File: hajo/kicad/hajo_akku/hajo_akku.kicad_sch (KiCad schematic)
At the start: 18 parts, among them J1 Seetalk NG, J2 Batteries, J4 Device type, U1 MCP2562, U2 LF50CV

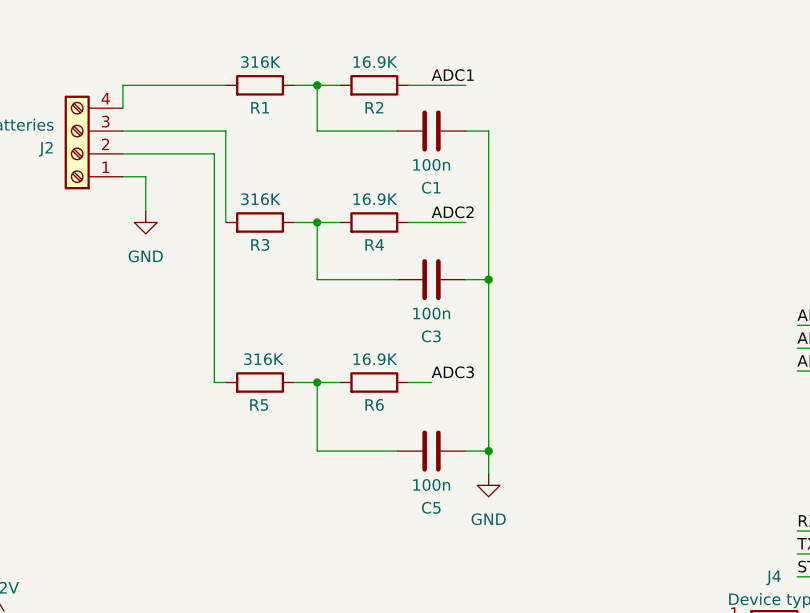
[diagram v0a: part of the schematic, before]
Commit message: kicad fix schematic
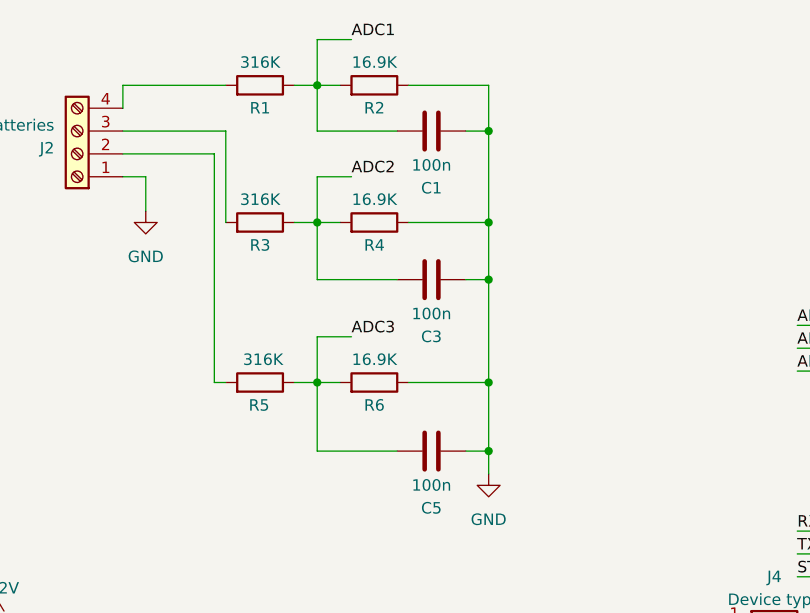
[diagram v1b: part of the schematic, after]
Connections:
- net ADC1: now also C1.2, R1.1, R2.2; no longer R2.1
- net ADC2: now also C3.2, R3.1, R4.2; no longer R4.1
- net ADC3: now also C5.2, R5.1, R6.2; no longer R6.1
- net GND: now also R2.1, R4.1, R6.1
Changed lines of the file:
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@@
   (junction (at 162.56 86.36) (diameter 0) (color 0 0 0 0)
   )
+  (junction (at 137.16 39.37) (diameter 0) (color 0 0 0 0)
+  )
   (junction (at 54.61 73.66) (diameter 0) (color 0 0 0 0)
   )
@@
   )
   (junction (at 25.4 73.66) (diameter 0) (color 0 0 0 0)
+  )
+  (junction (at 137.16 57.15) (diameter 0) (color 0 0 0 0)
+  )
+  (junction (at 137.16 29.21) (diameter 0) (color 0 0 0 0)
   )
   (junction (at 162.56 91.44) (diameter 0) (color 0 0 0 0)
@@
     (stroke (width 0) (type default))
   )
-  (wire (pts (xy 128.27 57.15) (xy 130.81 57.15))
-    (stroke (width 0) (type default))
-  )
   (wire (pts (xy 82.55 86.36) (xy 85.09 86.36))
     (stroke (width 0) (type default))
@@
     (stroke (width 0) (type default))
   )
-  (wire (pts (xy 137.16 45.72) (xy 137.16 64.77))
+  (wire (pts (xy 137.16 45.72) (xy 137.16 57.15))
     (stroke (width 0) (type default))
   )
@@
     (stroke (width 0) (type default))
   )
+  (wire (pts (xy 118.11 19.05) (xy 121.92 19.05))
+    (stroke (width 0) (type default))
+  )
   (wire (pts (xy 171.45 50.8) (xy 179.07 50.8))
     (stroke (width 0) (type default))
@@
     (stroke (width 0) (type default))
   )
+  (wire (pts (xy 118.11 24.13) (xy 118.11 19.05))
+    (stroke (width 0) (type default))
+  )
   (wire (pts (xy 107.95 39.37) (xy 107.95 29.21))
     (stroke (width 0) (type default))
@@
     (stroke (width 0) (type default))
   )
-  (wire (pts (xy 128.27 24.13) (xy 134.62 24.13))
-    (stroke (width 0) (type default))
-  )
   (wire (pts (xy 25.4 86.36) (xy 40.64 86.36))
     (stroke (width 0) (type default))
@@
     (stroke (width 0) (type default))
   )
+  (wire (pts (xy 137.16 57.15) (xy 137.16 64.77))
+    (stroke (width 0) (type default))
+  )
   (wire (pts (xy 85.09 96.52) (xy 82.55 96.52))
     (stroke (width 0) (type default))
@@
     (stroke (width 0) (type default))
   )
+  (wire (pts (xy 128.27 57.15) (xy 137.16 57.15))
+    (stroke (width 0) (type default))
+  )
+  (wire (pts (xy 128.27 24.13) (xy 137.16 24.13))
+    (stroke (width 0) (type default))
+  )
+  (wire (pts (xy 118.11 34.29) (xy 121.92 34.29))
+    (stroke (width 0) (type default))
+  )
   (wire (pts (xy 67.31 39.37) (xy 74.93 39.37))
     (stroke (width 0) (type default))
   )
+  (wire (pts (xy 118.11 39.37) (xy 118.11 34.29))
+    (stroke (width 0) (type default))
+  )
   (wire (pts (xy 120.65 24.13) (xy 118.11 24.13))
     (stroke (width 0) (type default))
   )
+  (wire (pts (xy 118.11 52.07) (xy 121.92 52.07))
+    (stroke (width 0) (type default))
+  )
   (wire (pts (xy 106.68 57.15) (xy 106.68 31.75))
     (stroke (width 0) (type default))
@@
     (stroke (width 0) (type default))
   )
-  (wire (pts (xy 137.16 29.21) (xy 137.16 45.72))
+  (wire (pts (xy 137.16 29.21) (xy 137.16 39.37))
     (stroke (width 0) (type default))
   )
@@
     (stroke (width 0) (type default))
   )
+  (wire (pts (xy 137.16 24.13) (xy 137.16 29.21))
+    (stroke (width 0) (type default))
+  )
   (wire (pts (xy 191.77 27.94) (xy 191.77 33.02))
     (stroke (width 0) (type default))
@@
     (stroke (width 0) (type default))
   )
+  (wire (pts (xy 118.11 57.15) (xy 118.11 52.07))
+    (stroke (width 0) (type default))
+  )
   (wire (pts (xy 96.52 24.13) (xy 96.52 26.67))
     (stroke (width 0) (type default))
   )
+  (wire (pts (xy 137.16 39.37) (xy 137.16 45.72))
+    (stroke (width 0) (type default))
+  )
   (wire (pts (xy 107.95 57.15) (xy 106.68 57.15))
     (stroke (width 0) (type default))
@@
     (stroke (width 0) (type default))
   )
-  (wire (pts (xy 128.27 39.37) (xy 134.62 39.37))
+  (wire (pts (xy 128.27 39.37) (xy 137.16 39.37))
     (stroke (width 0) (type default))
   )
@@
     (effects (font (size 1.27 1.27)) (justify left bottom))
   )
-  (label "ADC2" (at 130.81 39.37 0) (fields_autoplaced)
+  (label "ADC2" (at 121.92 34.29 0) (fields_autoplaced)
     (effects (font (size 1.27 1.27)) (justify left bottom))
   )
@@
     (effects (font (size 1.27 1.27)) (justify left bottom))
   )
-  (label "ADC1" (at 130.81 24.13 0) (fields_autoplaced)
-    (effects (font (size 1.27 1.27)) (justify left bottom))
-  )
-  (label "ADC3" (at 130.81 57.15 0) (fields_autoplaced)
-    (effects (font (size 1.27 1.27)) (justify left bottom))
-  )
+  (label "ADC1" (at 121.92 19.05 0) (fields_autoplaced)
+    (effects (font (size 1.27 1.27)) (justify left bottom))
+  )
+  (label "ADC3" (at 121.92 52.07 0) (fields_autoplaced)
+    (effects (font (size 1.27 1.27)) (justify left bottom))
+  )

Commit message: final pcb
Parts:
- removed J4: Device type, Connector_PinHeader_2.54mm:PinHeader_2x04_P2.54mm_Vertical, symbol Connector_Generic:Conn_02x04_Odd_Even
- added H1, H2, H3, H4: MountingHole, MountingHole:MountingHole_3.2mm_M3, symbol Mechanical:MountingHole
- added J3: Terminator, Connector_PinHeader_2.54mm:PinHeader_2x02_P2.54mm_Vertical, symbol Connector_Generic:Conn_02x02_Odd_Even
- U2: footprint Package_TO_SOT_THT:TO-220-3_Vertical -> Package_TO_SOT_THT:TO-220-3_Horizontal_TabDown
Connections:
- net CANH: now also J3.1 (Pin_1); no longer R7.1
- net CANL: now also J3.3 (Pin_3); no longer R7.2
- net GND: now also A1.16 (GPIO14/ADC2_3), J1.4 (Pin_4)
- new net: J3.2 (Pin_2), R7.1
- new net: J3.4 (Pin_4), R7.2
- no-connect marks 29 -> 31
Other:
- note added: "Shield"
- moved on the sheet: R7

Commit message: final pcb
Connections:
- net GND: now also A1.12 (GPIO10/ADC1_9); no longer A1.16 (GPIO14/ADC2_3)
- net RXD: now also A1.17 (GPIO15/ADC2_4/U0RTS); no longer A1.12 (GPIO10/ADC1_9)
- net STBY: now also A1.19 (GPIO17/ADC2_6/U1TXD); no longer A1.14 (GPIO12/ADC2_1)
- net TXD: now also A1.18 (GPIO16/ADC2_5/U0CTS); no longer A1.13 (GPIO11/ADC2_0)
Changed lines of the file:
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@@
   (junction (at 118.11 57.15) (diameter 0) (color 0 0 0 0)
   )
-  (no_connect (at 179.07 88.9))
+  (no_connect (at 179.07 78.74))
   (no_connect (at 229.87 78.74))
   (no_connect (at 229.87 66.04))
@@
   (no_connect (at 229.87 55.88))
   (no_connect (at 229.87 73.66))
-  (no_connect (at 179.07 86.36))
   (no_connect (at 229.87 93.98))
   (no_connect (at 229.87 86.36))
@@
   (no_connect (at 179.07 58.42))
   (no_connect (at 179.07 63.5))
+  (no_connect (at 179.07 83.82))
   (no_connect (at 229.87 68.58))
   (no_connect (at 229.87 58.42))
-  (no_connect (at 179.07 91.44))
+  (no_connect (at 179.07 76.2))
   (no_connect (at 179.07 71.12))
   (no_connect (at 179.07 68.58))
@@
     (stroke (width 0) (type default))
   )
-  (wire (pts (xy 171.45 76.2) (xy 179.07 76.2))
+  (wire (pts (xy 171.45 88.9) (xy 179.07 88.9))
     (stroke (width 0) (type default))
   )
@@
     (stroke (width 0) (type default))
   )
-  (wire (pts (xy 162.56 83.82) (xy 162.56 95.25))
-    (stroke (width 0) (type default))
-  )
   (wire (pts (xy 118.11 45.72) (xy 118.11 39.37))
     (stroke (width 0) (type default))
@@
     (stroke (width 0) (type default))
   )
-  (wire (pts (xy 162.56 83.82) (xy 179.07 83.82))
+  (wire (pts (xy 162.56 73.66) (xy 179.07 73.66))
     (stroke (width 0) (type default))
   )
@@
     (stroke (width 0) (type default))
   )
-  (wire (pts (xy 171.45 78.74) (xy 179.07 78.74))
+  (wire (pts (xy 171.45 91.44) (xy 179.07 91.44))
     (stroke (width 0) (type default))
   )
@@
     (stroke (width 0) (type default))
   )
-  (wire (pts (xy 171.45 73.66) (xy 179.07 73.66))
+  (wire (pts (xy 171.45 86.36) (xy 179.07 86.36))
     (stroke (width 0) (type default))
   )
@@
     (effects (font (size 1.27 1.27)) (justify left bottom))
   )
-  (label "RXD" (at 171.45 73.66 0) (fields_autoplaced)
+  (label "RXD" (at 171.45 86.36 0) (fields_autoplaced)
     (effects (font (size 1.27 1.27)) (justify left bottom))
   )
@@
     (effects (font (size 1.27 1.27)) (justify left bottom))
   )
-  (label "TXD" (at 171.45 76.2 0) (fields_autoplaced)
+  (label "TXD" (at 171.45 88.9 0) (fields_autoplaced)
     (effects (font (size 1.27 1.27)) (justify left bottom))
   )
@@
     (effects (font (size 1.27 1.27)) (justify left bottom))
   )
-  (label "STBY" (at 171.45 78.74 0) (fields_autoplaced)
+  (label "STBY" (at 171.45 91.44 0) (fields_autoplaced)
     (effects (font (size 1.27 1.27)) (justify left bottom))
   )
@@
     )
   )
-  (symbol (lib_id "power:GND") (at 162.56 95.25 0) (unit 1)
-    (in_bom yes) (on_board yes) (dnp no) (fields_autoplaced)
-    (property "Reference" "#PWR014" (at 162.56 101.6 0)
-      (effects (font (size 1.27 1.27)) hide)
-    )
-    (property "Value" "GND" (at 162.56 100.33 0)
-      (effects (font (size 1.27 1.27)))
-    )
-    (property "Footprint" "" (at 162.56 95.25 0)
-      (effects (font (size 1.27 1.27)) hide)
-    )
-    (property "Datasheet" "" (at 162.56 95.25 0)
-      (effects (font (size 1.27 1.27)) hide)
-    )
+  (symbol (lib_id "power:GND") (at 162.56 73.66 0) (unit 1)
+    (in_bom yes) (on_board yes) (dnp no) (fields_autoplaced)
+    (property "Reference" "#PWR014" (at 162.56 80.01 0)
+      (effects (font (size 1.27 1.27)) hide)
+    )
+    (property "Value" "GND" (at 162.56 78.74 0)
+      (effects (font (size 1.27 1.27)))
+    )
+    (property "Footprint" "" (at 162.56 73.66 0)
+      (effects (font (size 1.27 1.27)) hide)
+    )
+    (property "Datasheet" "" (at 162.56 73.66 0)
+      (effects (font (size 1.27 1.27)) hide)
+    )

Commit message: fix akku
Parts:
- U1: footprint Package_DIP:DIP-8_W7.62mm -> Package_DIP:DIP-8_W7.62mm_Socket
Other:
- moved on the sheet: C3, C5, R3, R4, R5, R6

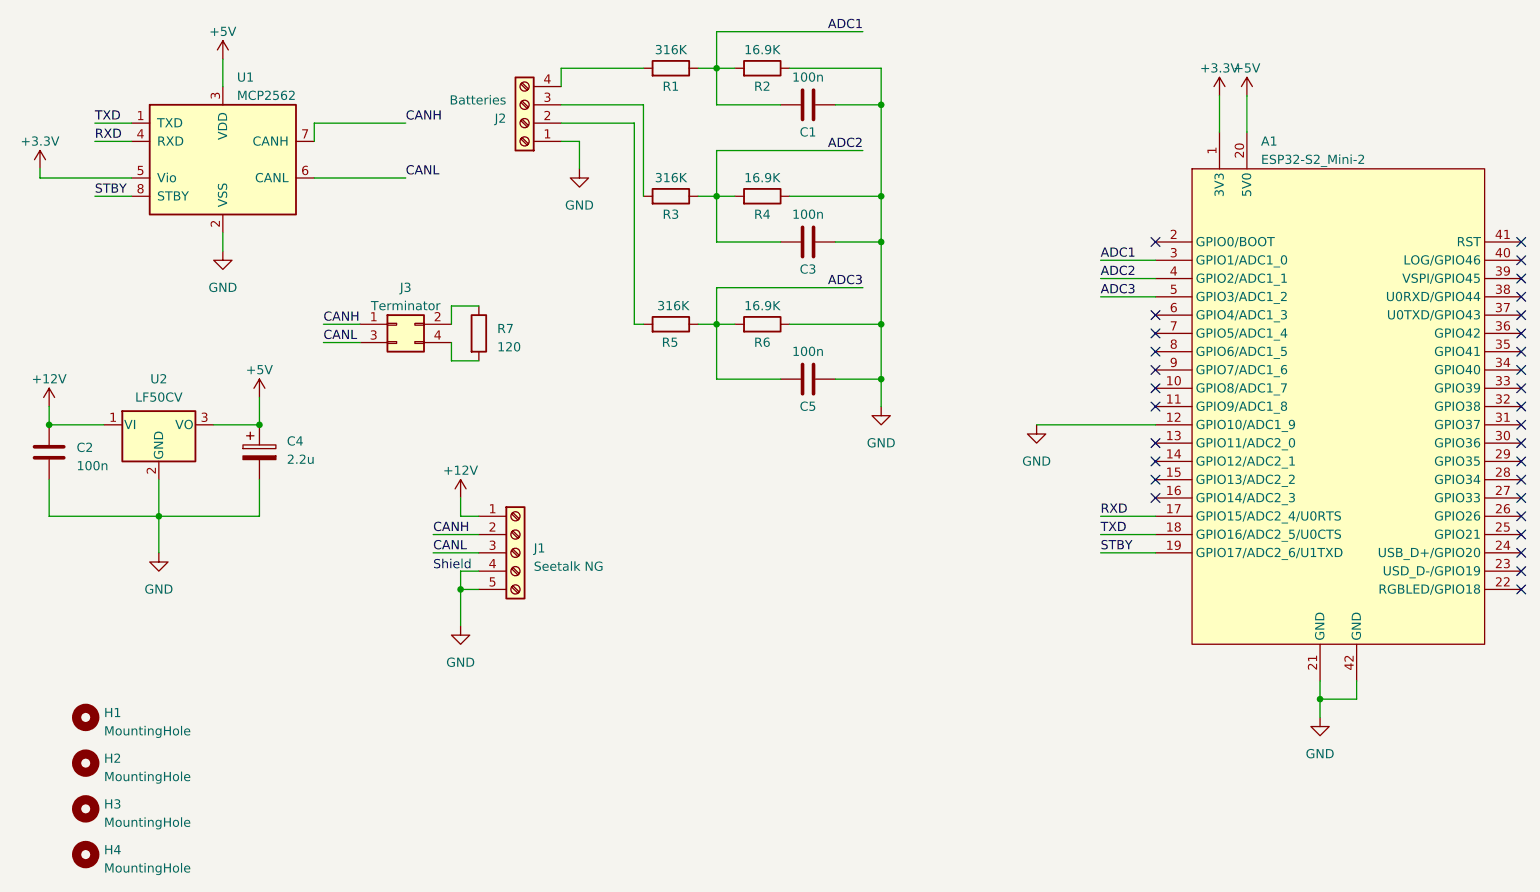
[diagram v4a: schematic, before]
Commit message: akku on new board
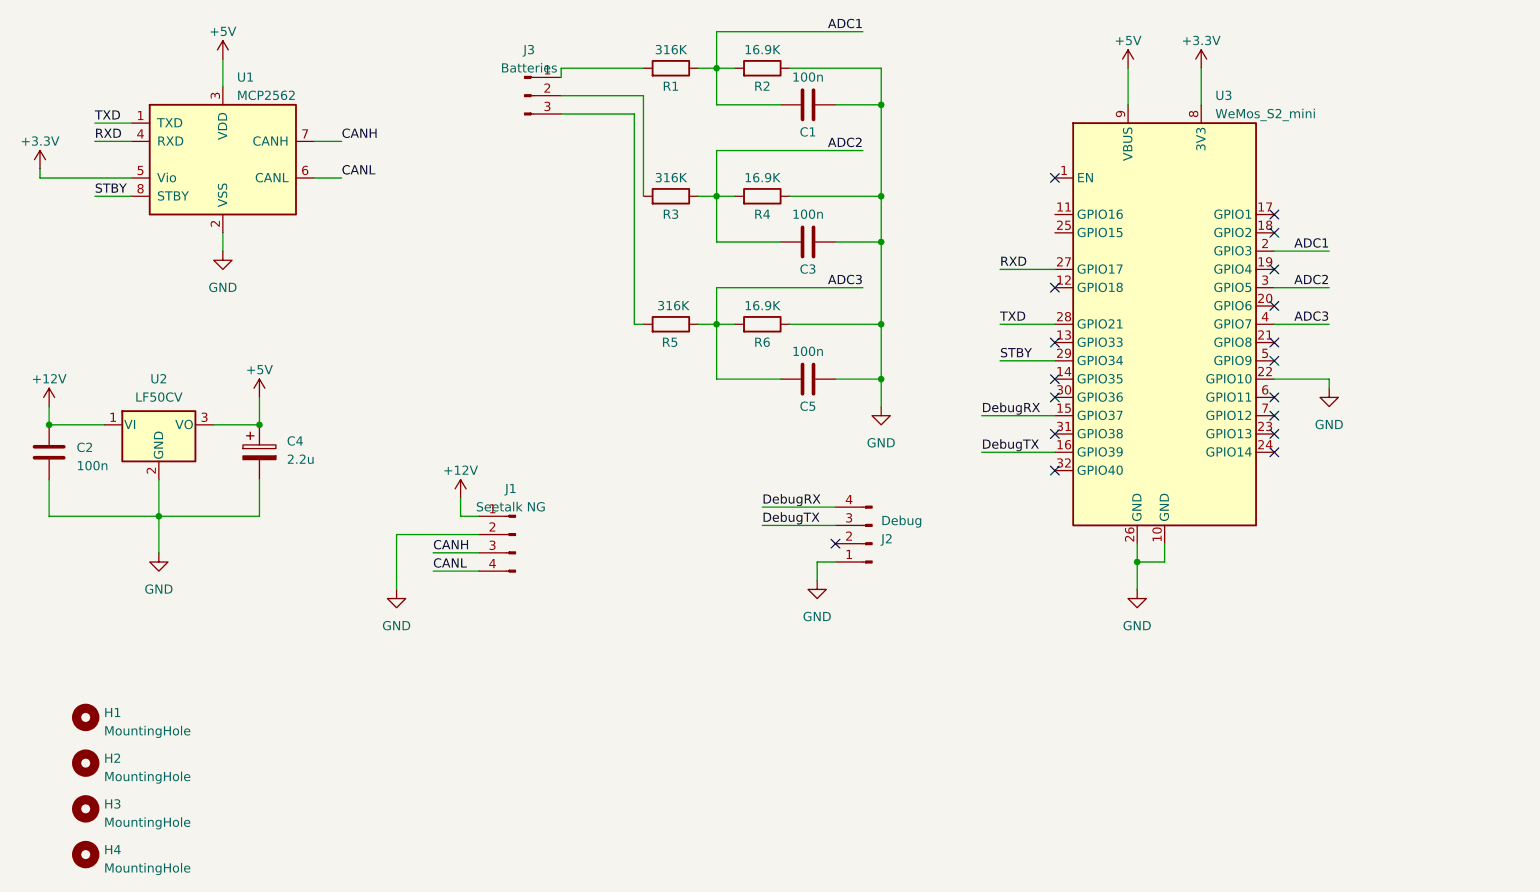
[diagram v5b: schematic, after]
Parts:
- removed A1: ESP32-S2_Mini-2, own:DIP-42_W15.24mm, symbol own:ESP32-S2_Mini-2
- removed J1: Seetalk NG, Connector_Phoenix_MC_HighVoltage:PhoenixContact_MCV_1,5_5-G-5.08_1x05_P5.08mm_Vertical, symbol Connector:Screw_Terminal_01x05
- removed J2: Batteries, Connector_Phoenix_MC_HighVoltage:PhoenixContact_MCV_1,5_4-G-5.08_1x04_P5.08mm_Vertical, symbol Connector:Screw_Terminal_01x04
- removed J3: Terminator, Connector_PinHeader_2.54mm:PinHeader_2x02_P2.54mm_Vertical, symbol Connector_Generic:Conn_02x02_Odd_Even
- removed R7: 120, Resistor_THT:R_Axial_DIN0207_L6.3mm_D2.5mm_P7.62mm_Horizontal, symbol Device:R
- added J1: Seetalk NG, Connector_PinHeader_2.54mm:PinHeader_1x04_P2.54mm_Vertical, symbol Connector:Conn_01x04_Pin
- added J2: Debug, Connector_PinHeader_2.54mm:PinHeader_1x04_P2.54mm_Vertical, symbol Connector:Conn_01x04_Pin
- added J3: Batteries, Connector_PinHeader_2.54mm:PinHeader_1x03_P2.54mm_Vertical, symbol Connector:Conn_01x03_Pin
- added U3: WeMos_S2_mini, own:WEMOS_S2_mini_traced, symbol own:WeMos_S2_mini
- U2: footprint Package_TO_SOT_THT:TO-220-3_Horizontal_TabDown -> Package_TO_SOT_THT:TO-220-3_Vertical
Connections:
- net +12V: now also J1.1 (Pin_1)
- net +3.3V: now also U3.8 (3V3)
- net +5V: now also U3.9 (VBUS)
- net ADC1: now also U3.2 (GPIO3)
- net ADC2: now also U3.3 (GPIO5)
- net ADC3: now also U3.4 (GPIO7)
- net CANH: now also J1.3 (Pin_3)
- net CANL: now also J1.4 (Pin_4)
- net GND: now also J1.2 (Pin_2), J2.1 (Pin_1), U3.10 (GND), U3.22 (GPIO10), U3.26 (GND)
- net RXD: now also U3.27 (GPIO17)
- net STBY: now also U3.29 (GPIO34)
- net TXD: now also U3.28 (GPIO21)
- net at R1.2: now also J3.1 (Pin_1)
- net at R5.2: now also J3.3 (Pin_3)
- net at R3.2: now also J3.2 (Pin_2)
- new net DebugRX: J2.4 (Pin_4), U3.15 (GPIO37)
- new net DebugTX: J2.3 (Pin_3), U3.16 (GPIO39)
- no-connect marks 31 -> 18
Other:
- note removed: "Shield"
